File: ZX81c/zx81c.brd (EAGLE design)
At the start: 142 x 100 mm, 72 parts, among them IC1 ZX81ULA, IC2 27C512, IC2B ZXROM-SMALL, IC3 Z80CPU, IC4 62256, IC4A 2114, IC4B 2114, K1 ZX81CONN, K2 MIC, K3 EAR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

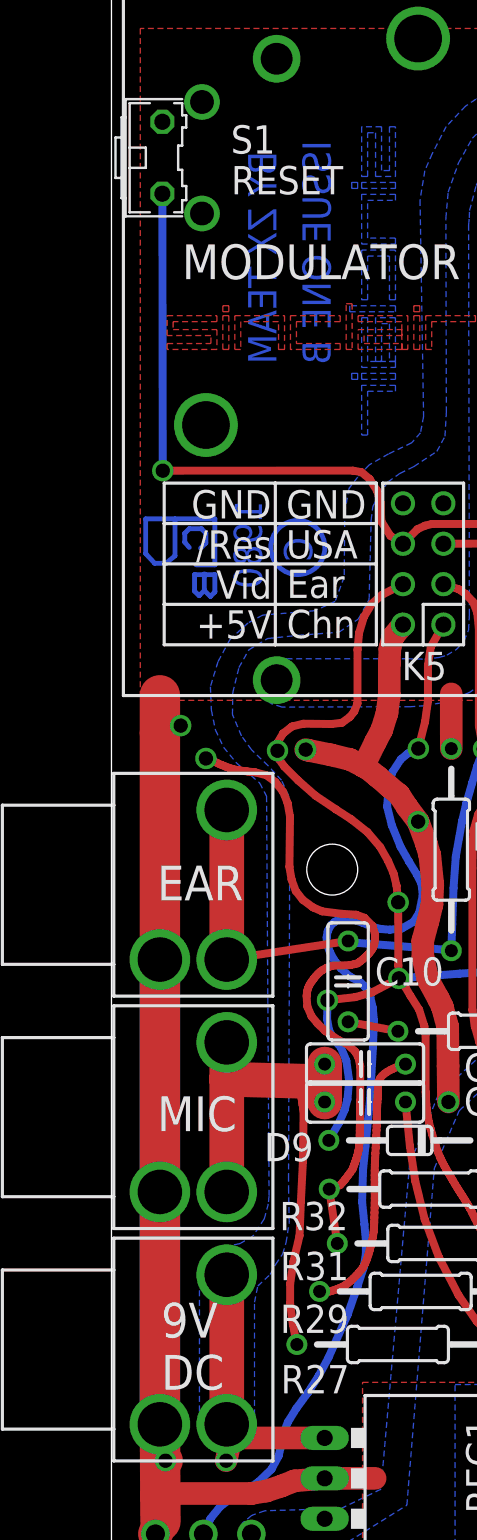
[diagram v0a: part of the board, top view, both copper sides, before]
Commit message: Add files via upload
Changed connectors to 4 pin version. Corrected Issue 3 C string and added a year
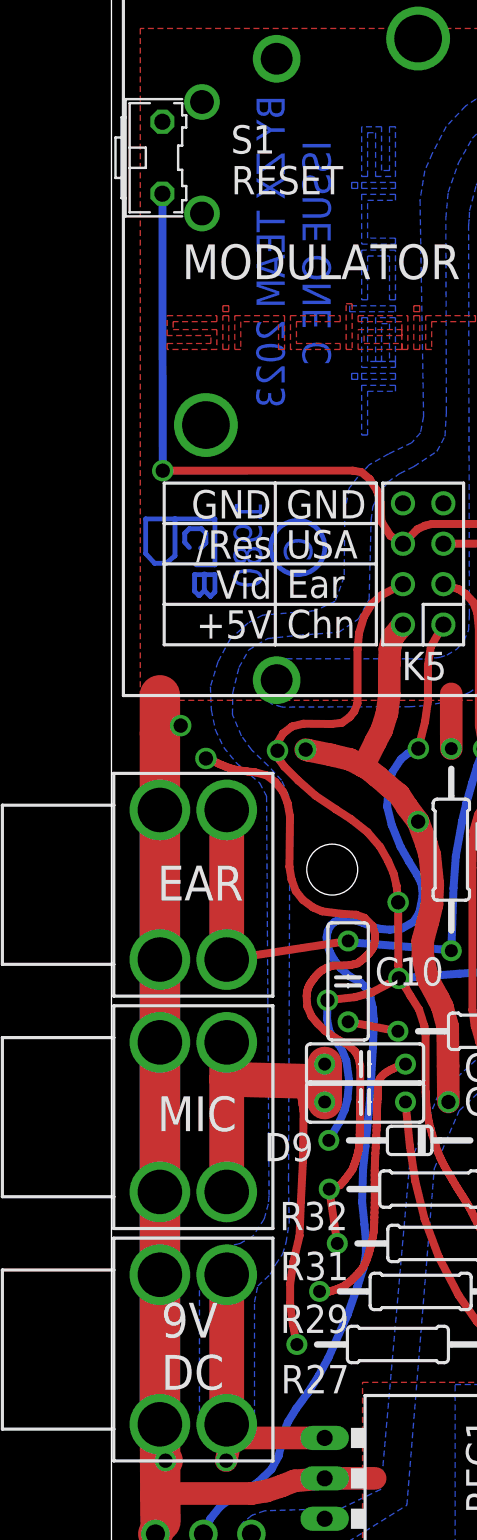
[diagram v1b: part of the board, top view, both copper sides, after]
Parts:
- K2, K3, K4: device sinclair:ZXKLINKE -> sinclair:ZXKLINKE4POL
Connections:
- net GND: now also K2.2', K3.2', K4.2'
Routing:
- net GND: track 227.5 -> 236.9 mm
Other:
- board text added: "BY ZX TEAM 2023"
- board text added: "ISSUE ONE C"
- board text removed: "BY ZX TEAM"
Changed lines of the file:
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@@
 <text x="12.620503125" y="64.715996875" size="1.778" layer="16" rot="SMR270">C</text>
 <circle x="11.711084375" y="64.052415625" radius="1.70018125" width="0.3048" layer="16"/>
-<text x="13.782375" y="89.63179375" size="1.778" layer="16" rot="SMR270">ISSUE ONE B</text>
+<text x="13.782375" y="89.63179375" size="1.778" layer="16" rot="SMR270">ISSUE ONE C</text>
 <wire x1="0.75" y1="99.25" x2="25.125" y2="99.25" width="0.2" layer="21"/>
 <wire x1="25.125" y1="99.25" x2="25.125" y2="54.75" width="0.2" layer="21"/>
@@
 <rectangle x1="15.875" y1="0.25" x2="32.125" y2="11.375" layer="29"/>
 <text x="125" y="15.5" size="1.778" layer="21">D1 - D8</text>
-<text x="10.36809375" y="88.954759375" size="1.778" layer="16" rot="SMR270">BY ZX TEAM</text>
+<text x="10.890278125" y="92.46304375" size="1.778" layer="16" rot="SMR270">BY ZX TEAM 2023</text>
 <wire x1="88.7" y1="92" x2="90.5" y2="92" width="0" layer="20"/>
 <text x="10.07748125" y="65.130703125" size="1.778" layer="21" rot="R180">/Res</text>
@@
 <element name="KB1" library="sinclair" package="ZXKDB5" value="ZXKBD5CON" x="107.37875" y="2.21875" rot="R180"/>
 <element name="KB2" library="sinclair" package="ZXKBD8" value="ZXKBD8CON" x="128.96875" y="4.12375"/>
-<element name="K4" library="sinclair" package="ZXKLINKE" value="DCIN" x="5.14375" y="13.64875"/>
-<element name="K3" library="sinclair" package="ZXKLINKE" value="EAR" x="5.14375" y="42.85875"/>
-<element name="K2" library="sinclair" package="ZXKLINKE" value="MIC" x="5.14375" y="28.25375"/>
+<element name="K4" library="sinclair" package="ZXKLINKE4POL" value="DCIN" x="5.14375" y="13.64875"/>
+<element name="K3" library="sinclair" package="ZXKLINKE4POL" value="EAR" x="5.14375" y="42.85875"/>
+<element name="K2" library="sinclair" package="ZXKLINKE4POL" value="MIC" x="5.14375" y="28.25375"/>
 <element name="RP4" library="sinclair" package="SIL8P" value="470" x="51.125" y="50.75" smashed="yes" rot="R270">
 <attribute name="VALUE" x="52.395" y="53.29" size="1.27" layer="27" ratio="10" rot="R270"/>
@@
 <wire x1="27.084559375" y1="20.073459375" x2="26.8925" y2="20.31625" width="0.5" layer="1"/>
 <wire x1="26.8925" y1="20.31625" x2="25.78125" y2="21.58625" width="0.5" layer="1"/>
-<wire x1="3.04375" y1="23.55375" x2="3.04375" y2="38.15875" width="2.54" layer="1"/>
+<wire x1="3.04375" y1="23.55375" x2="3.04375" y2="32.95375" width="2.54" layer="1"/>
 <via x="4.35" y="52.86" extent="1-16" drill="0.9"/>
 <via x="10.3825" y="55.7175" extent="1-16" drill="2"/>
@@
 <wire x1="22.962315625" y1="15.40935625" x2="24.3525" y2="13.96625" width="0.5" layer="1"/>
 <wire x1="3.04375" y1="38.15875" x2="3.04375" y2="52.375" width="2.54" layer="1"/>
-<wire x1="3.04375" y1="8.94875" x2="3.04375" y2="23.55375" width="2.54" layer="1"/>
+<wire x1="3.04375" y1="8.94875" x2="3.04375" y2="18.34875" width="2.54" layer="1"/>
 <contactref element="K5" pad="8"/>
 <contactref element="K5" pad="7"/>
@@
 <wire x1="92.057125" y1="12.562334375" x2="91.201684375" y2="12.966225" width="0.5" layer="16"/>
 <wire x1="120.074953125" y1="9.2144375" x2="122.614953125" y2="9.2144375" width="0.5" layer="16"/>
+<contactref element="K2" pad="2'"/>
+<contactref element="K3" pad="2'"/>
+<wire x1="3.04375" y1="38.15875" x2="3.04375" y2="47.55875" width="2.54" layer="16"/>
+<wire x1="3.04375" y1="38.15875" x2="3.04375" y2="32.95375" width="2.54" layer="1"/>
+<contactref element="K4" pad="2'"/>
+<wire x1="3.04375" y1="18.34875" x2="3.04375" y2="23.55375" width="2.54" layer="1"/>
 </signal>
 <signal name="A0">
